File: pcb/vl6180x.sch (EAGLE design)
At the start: 5 parts, among them J1 6PINBOARDEDGE, U1 STPROXSENSOR

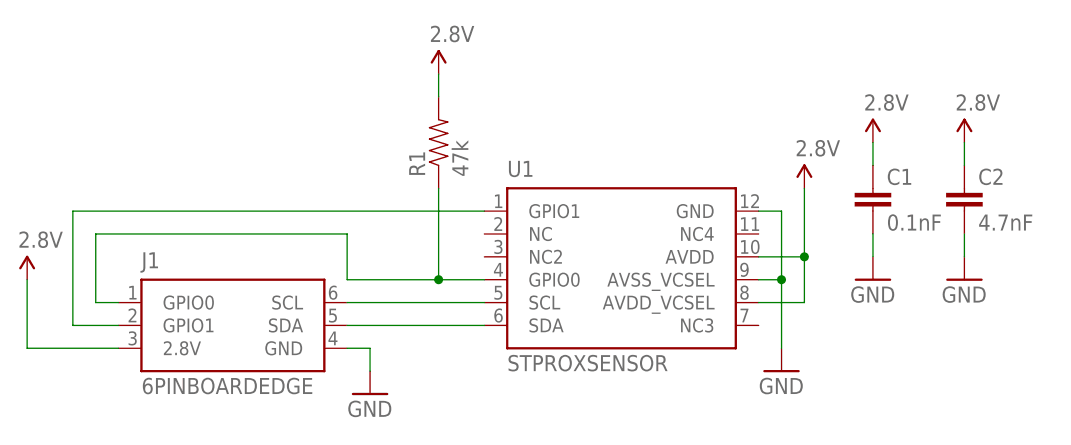
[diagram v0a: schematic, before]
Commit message: Fixed 2.8v regulator pinout
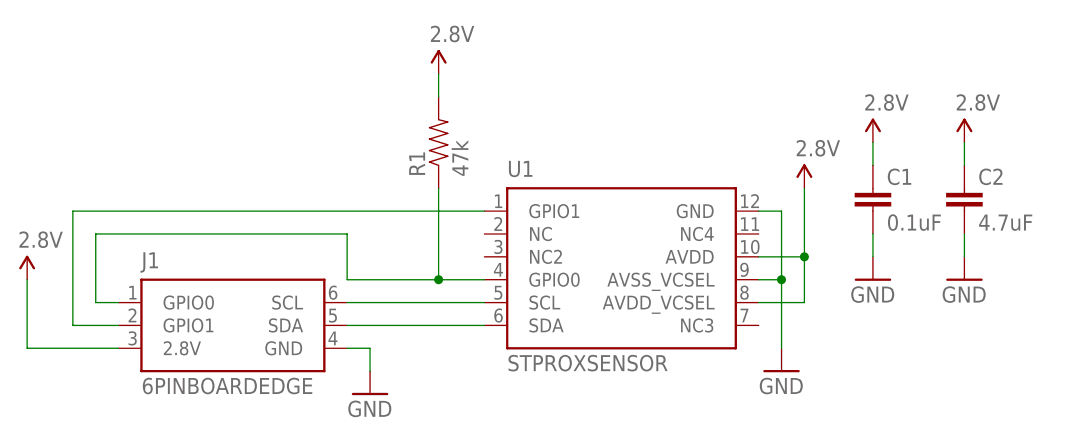
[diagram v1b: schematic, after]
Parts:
- C1: value 0.1nF -> 0.1uF
- C2: value 4.7nF -> 4.7uF
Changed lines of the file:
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@@
 <parts>
 <part name="U1" library="Nick'sEagle" deviceset="STPROXSENSOR" device=""/>
-<part name="C1" library="SparkFun-Passives" deviceset="CAP" device="0603-CAP" value="0.1nF"/>
-<part name="C2" library="SparkFun-Passives" deviceset="CAP" device="0603-CAP" value="4.7nF"/>
+<part name="C1" library="SparkFun-Passives" deviceset="CAP" device="0603-CAP" value="0.1uF"/>
+<part name="C2" library="SparkFun-Passives" deviceset="CAP" device="0603-CAP" value="4.7uF"/>
 <part name="R1" library="SparkFun-Passives" deviceset="RESISTOR" device="0603-RES" value="47k"/>
 <part name="SUPPLY1" library="SparkFun-Aesthetics" deviceset="2.8V" device=""/>
